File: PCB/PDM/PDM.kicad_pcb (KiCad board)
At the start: 2 copper layers, 42 parts, among them IC1 BTS70021EPPXUMA1, IC2 BTS70021EPPXUMA1, IC3 BTS500101TAEATMA1, IC4 TS5A21366DCUR, Q1 MMBT3904, U1 STM32F405RGTx, U2 MCP2561-E-SN, U3 MCP2561-E-SN

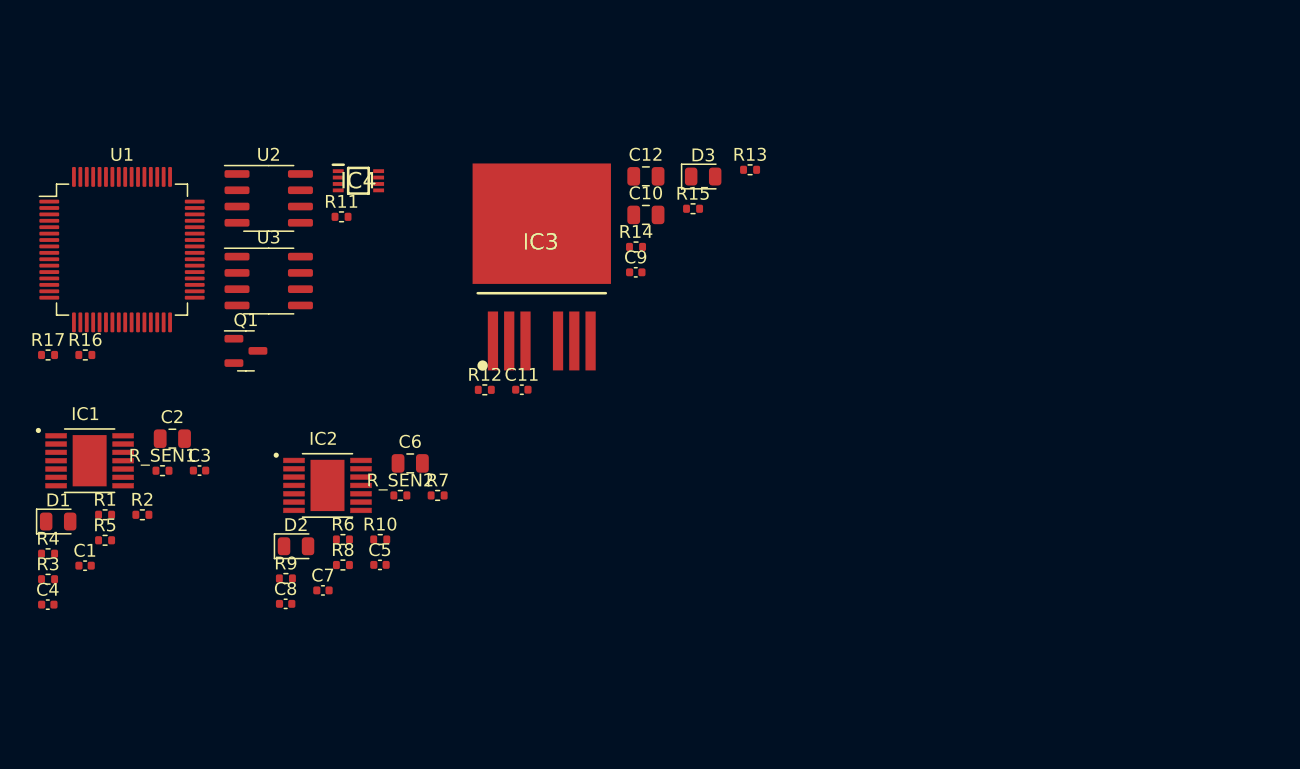
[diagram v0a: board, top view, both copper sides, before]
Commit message: Added another high-side switch 2x7A + 2x4A SPI
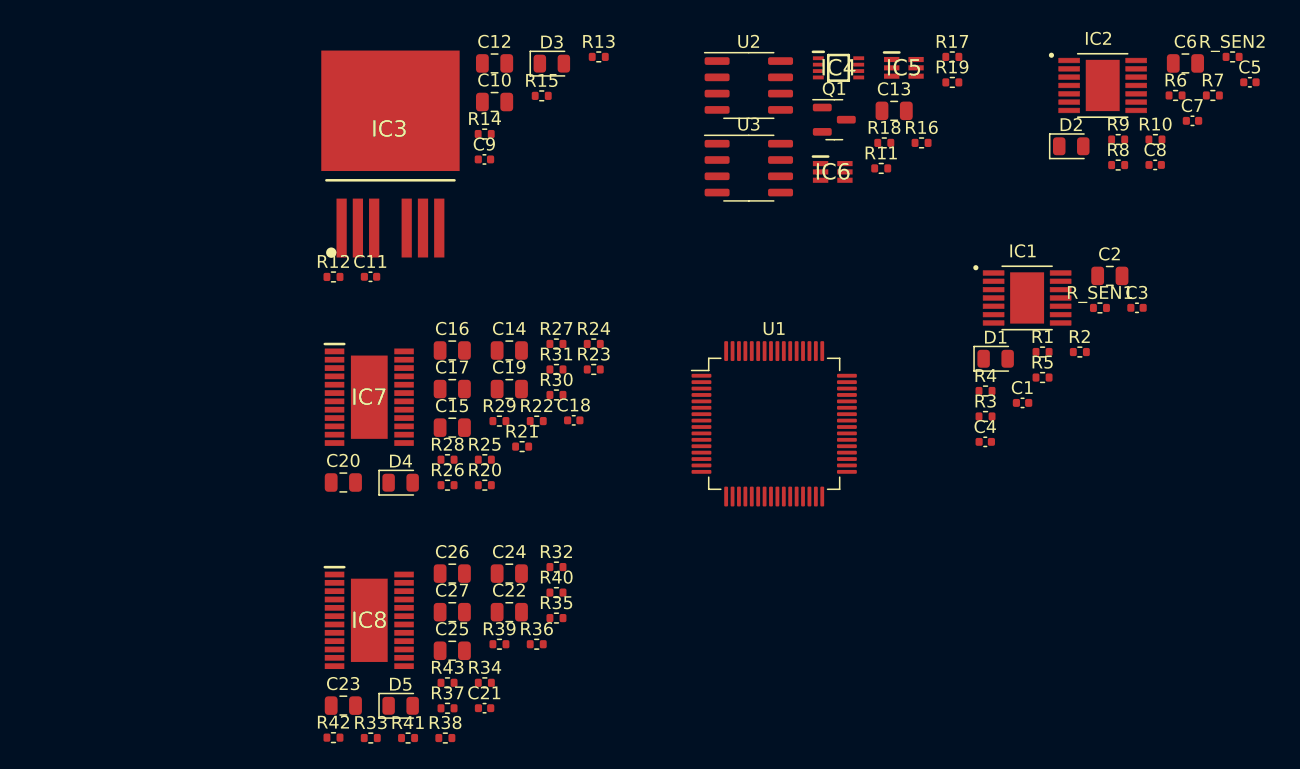
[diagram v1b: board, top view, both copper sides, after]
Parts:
- added C13: 0,1mF, Capacitor_SMD:C_0805_2012Metric, F.Cu at (245.5, 23.9)
- added C14: 10nf, Capacitor_SMD:C_0805_2012Metric, F.Cu at (215.5, 42.6)
- added C15: 10nf, Capacitor_SMD:C_0805_2012Metric, F.Cu at (211.0, 48.7)
- added C16: 10nf, Capacitor_SMD:C_0805_2012Metric, F.Cu at (211.0, 42.6)
- added C17: 10nf, Capacitor_SMD:C_0805_2012Metric, F.Cu at (211.0, 45.7)
- added C18: 220pF, Capacitor_SMD:C_0402_1005Metric, F.Cu at (220.5, 48.1)
- added C19: 470nF, Capacitor_SMD:C_0805_2012Metric, F.Cu at (215.5, 45.7)
- added C20: 100nF, Capacitor_SMD:C_0805_2012Metric, F.Cu at (202.5, 52.9)
- added C21: 220pF, Capacitor_SMD:C_0402_1005Metric, F.Cu at (213.5, 70.6)
- added C22: 470nF, Capacitor_SMD:C_0805_2012Metric, F.Cu at (215.5, 63.1)
- added C23: 100nF, Capacitor_SMD:C_0805_2012Metric, F.Cu at (202.5, 70.4)
- added C24: 10nf, Capacitor_SMD:C_0805_2012Metric, F.Cu at (215.5, 60.1)
- added C25: 10nf, Capacitor_SMD:C_0805_2012Metric, F.Cu at (211.0, 66.1)
- added C26: 10nf, Capacitor_SMD:C_0805_2012Metric, F.Cu at (211.0, 60.1)
- added C27: 10nf, Capacitor_SMD:C_0805_2012Metric, F.Cu at (211.0, 63.1)
- added D4: 7V, Diode_SMD:D_0805_2012Metric, F.Cu at (207.0, 53.0)
- added D5: 7V, Diode_SMD:D_0805_2012Metric, F.Cu at (207.0, 70.4)
- added IC5: TMP126NDCKR, PDM_Additional:SOT65P210X110-6N, F.Cu at (246.3, 20.6)
- added IC6: TMP126NDCKR, PDM_Additional:SOT65P210X110-6N, F.Cu at (240.7, 28.7)
- added IC7: BTS722204ESAXUMA1, PDM_Additional:SOP65P600X115-25N, F.Cu at (204.5, 46.3)
- added IC8: BTS722204ESAXUMA1, PDM_Additional:SOP65P600X115-25N, F.Cu at (204.5, 63.7)
- added R18: 10k, Resistor_SMD:R_0402_1005Metric, F.Cu at (244.7, 26.4)
- added R19: 10k, Resistor_SMD:R_0402_1005Metric, F.Cu at (250.0, 21.7)
- added R20: 1.2k, Resistor_SMD:R_0402_1005Metric, F.Cu at (213.6, 53.2)
- added R21: 1.2k, Resistor_SMD:R_0402_1005Metric, F.Cu at (216.5, 50.1)
- added R22: 1.2k, Resistor_SMD:R_0402_1005Metric, F.Cu at (217.6, 48.2)
- added R23: 1.2k, Resistor_SMD:R_0402_1005Metric, F.Cu at (222.1, 44.1)
- added R24: 4.7k, Resistor_SMD:R_0402_1005Metric, F.Cu at (222.1, 42.1)
- added R25: 4.7k, Resistor_SMD:R_0402_1005Metric, F.Cu at (213.6, 51.2)
- added R26: 4.7k, Resistor_SMD:R_0402_1005Metric, F.Cu at (210.7, 53.2)
- added R27: 4.7k, Resistor_SMD:R_0402_1005Metric, F.Cu at (219.2, 42.1)
- added R28: 47, Resistor_SMD:R_0402_1005Metric, F.Cu at (210.7, 51.2)
- added R29: 470, Resistor_SMD:R_0402_1005Metric, F.Cu at (214.7, 48.2)
- added R30: 4.7k, Resistor_SMD:R_0402_1005Metric, F.Cu at (219.2, 46.1)
- added R31: 1.2k, Resistor_SMD:R_0402_1005Metric, F.Cu at (219.2, 44.1)
- added R32: 47, Resistor_SMD:R_0402_1005Metric, F.Cu at (219.2, 59.5)
- added R33: 470, Resistor_SMD:R_0402_1005Metric, F.Cu at (204.7, 72.9)
- added R34: 4.7k, Resistor_SMD:R_0402_1005Metric, F.Cu at (213.6, 68.6)
- added R35: 1.2k, Resistor_SMD:R_0402_1005Metric, F.Cu at (219.2, 63.5)
- added R36: 1.2k, Resistor_SMD:R_0402_1005Metric, F.Cu at (217.6, 65.6)
- added R37: 1.2k, Resistor_SMD:R_0402_1005Metric, F.Cu at (210.7, 70.6)
- added R38: 1.2k, Resistor_SMD:R_0402_1005Metric, F.Cu at (210.5, 72.9)
- added R39: 4.7k, Resistor_SMD:R_0402_1005Metric, F.Cu at (214.7, 65.6)
- added R40: 4.7k, Resistor_SMD:R_0402_1005Metric, F.Cu at (219.2, 61.5)
- added R41: 4.7k, Resistor_SMD:R_0402_1005Metric, F.Cu at (207.6, 72.9)
- added R42: 4.7k, Resistor_SMD:R_0402_1005Metric, F.Cu at (201.8, 72.9)
- added R43: 1.2k, Resistor_SMD:R_0402_1005Metric, F.Cu at (210.7, 68.6)
- moved C5 77.6 mm to (273.3, 21.7)
- moved C7 77.1 mm to (268.8, 24.7)
- moved C8 76.0 mm to (265.9, 28.2)
- moved R17 74.3 mm to (250.0, 19.7)
- moved C2 74.2 mm to (262.3, 36.8)
- moved C3 74.2 mm to (264.5, 39.3)
- moved C4 74.2 mm to (252.6, 49.8)
- moved D1 74.2 mm to (253.4, 43.3)
- moved R1 74.2 mm to (257.1, 42.8)
- moved R2 74.2 mm to (260.0, 42.8)
- moved R5 74.2 mm to (257.1, 44.8)
- moved R_SEN1 74.2 mm to (261.6, 39.3)
- moved C1 74.2 mm to (255.5, 46.7)
- moved IC1 74.2 mm to (255.9, 38.5)
- moved R3 74.2 mm to (252.6, 47.8)
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
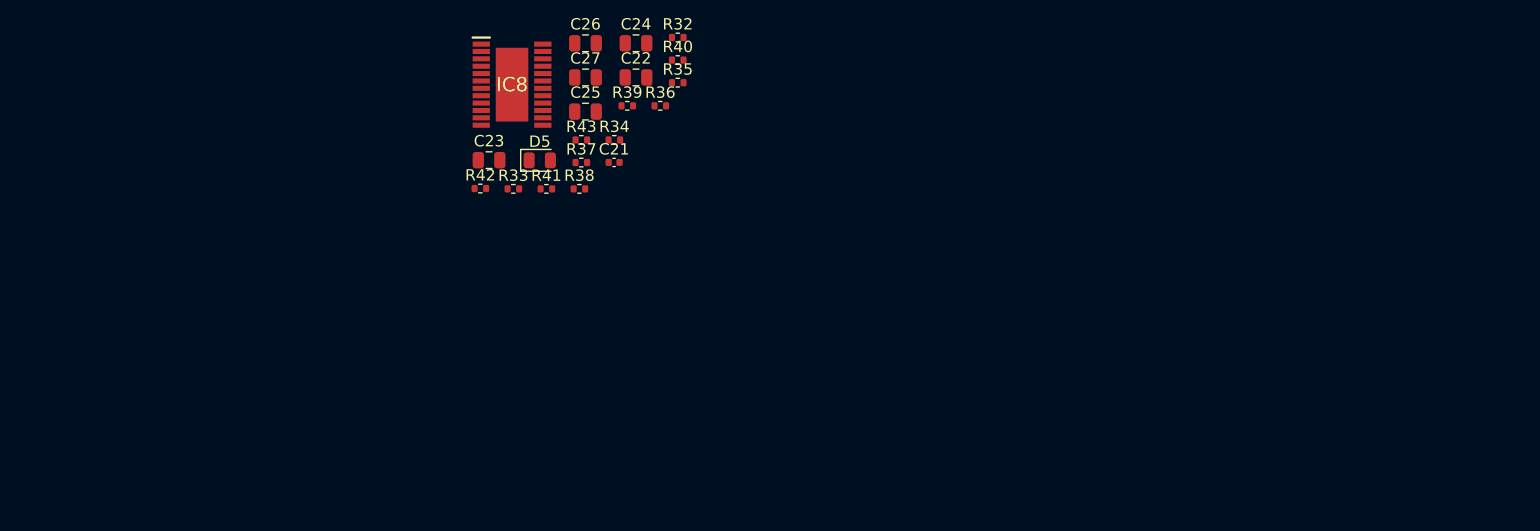
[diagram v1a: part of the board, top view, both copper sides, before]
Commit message: Added Reverse polarity protection
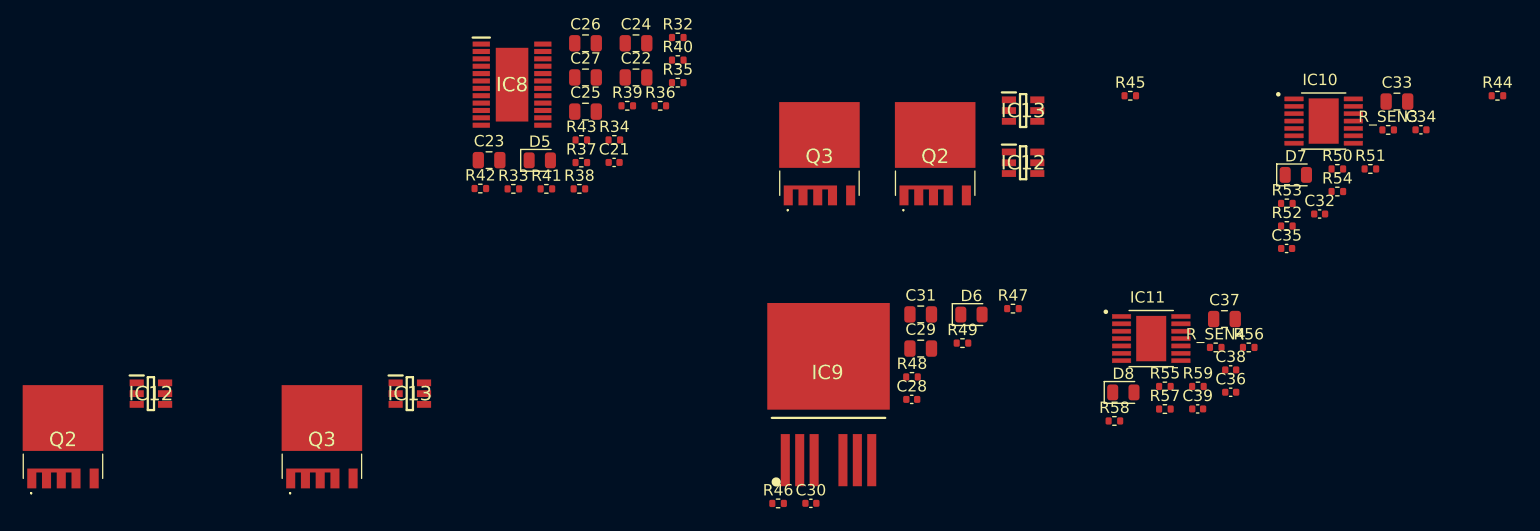
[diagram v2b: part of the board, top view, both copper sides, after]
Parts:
- added C28: 10nF, Capacitor_SMD:C_0402_1005Metric, F.Cu at (239.8, 91.4)
- added C29: 150nF, Capacitor_SMD:C_0805_2012Metric, F.Cu at (240.6, 87.0)
- added C30: 10nF, Capacitor_SMD:C_0402_1005Metric, F.Cu at (230.9, 100.6)
- added C31: 100nF, Capacitor_SMD:C_0805_2012Metric, F.Cu at (240.6, 84.0)
- added C32: 220pF, Capacitor_SMD:C_0402_1005Metric, F.Cu at (275.7, 75.1)
- added C33: 100nF, Capacitor_SMD:C_0805_2012Metric, F.Cu at (282.5, 65.2)
- added C34: 47nF, Capacitor_SMD:C_0402_1005Metric, F.Cu at (284.7, 67.7)
- added C35: 10nF, Capacitor_SMD:C_0402_1005Metric, F.Cu at (272.8, 78.1)
- added C36: 220pF, Capacitor_SMD:C_0402_1005Metric, F.Cu at (267.9, 90.8)
- added C37: 100nF, Capacitor_SMD:C_0805_2012Metric, F.Cu at (267.3, 84.4)
- added C38: 47nF, Capacitor_SMD:C_0402_1005Metric, F.Cu at (267.9, 88.8)
- added C39: 10nF, Capacitor_SMD:C_0402_1005Metric, F.Cu at (265.0, 92.3)
- added D6: 40V, Diode_SMD:D_0805_2012Metric, F.Cu at (245.0, 84.0)
- added D7: 7V, Diode_SMD:D_0805_2012Metric, F.Cu at (273.6, 71.7)
- added D8: 7V, Diode_SMD:D_0805_2012Metric, F.Cu at (258.4, 90.8)
- added IC10: BTS70021EPPXUMA1, PDM_Additional:SOP65P600X115-15N, F.Cu at (276.1, 66.9)
- added IC11: BTS70021EPPXUMA1, PDM_Additional:SOP65P600X115-15N, F.Cu at (260.9, 86.1)
- added IC12: LM5050MK-1_NOPB, PDM_Additional:SOT95P280X110-6N, F.Cu at (172.7, 90.9)
- added IC12: LM5050MK-1_NOPB, PDM_Additional:SOT95P280X110-6N, F.Cu at (249.6, 70.6)
- added IC13: LM5050MK-1_NOPB, PDM_Additional:SOT95P280X110-6N, F.Cu at (249.6, 66.0)
- added IC13: LM5050MK-1_NOPB, PDM_Additional:SOT95P280X110-6N, F.Cu at (195.5, 90.9)
- added IC9: BTS500101TAEATMA1, PDM_Additional:PG-TO263-7-3_3, F.Cu at (232.4, 87.6)
- added Q2: IAUA250N04S6N007AUMA1, PDM_Additional:IAUA250N04S6N007AUMA1, F.Cu at (241.8, 71.0)
- added Q2: IAUA250N04S6N007AUMA1, PDM_Additional:IAUA250N04S6N007AUMA1, F.Cu at (165.0, 96.0)
- added Q3: IAUA250N04S6N007AUMA1, PDM_Additional:IAUA250N04S6N007AUMA1, F.Cu at (231.6, 71.0)
- added Q3: IAUA250N04S6N007AUMA1, PDM_Additional:IAUA250N04S6N007AUMA1, F.Cu at (187.8, 96.0)
- added R44: 1.2k, Resistor_SMD:R_0402_1005Metric, F.Cu at (291.4, 64.7)
- added R45: 1.2k, Resistor_SMD:R_0402_1005Metric, F.Cu at (259.0, 64.7)
- added R46: 4.7k, Resistor_SMD:R_0402_1005Metric, F.Cu at (228.0, 100.6)
- added R47: 1k, Resistor_SMD:R_0402_1005Metric, F.Cu at (248.7, 83.4)
- added R48: 4.7k, Resistor_SMD:R_0402_1005Metric, F.Cu at (239.8, 89.5)
- added R49: 10, Resistor_SMD:R_0402_1005Metric, F.Cu at (244.2, 86.5)
- added R50: 4,7k, Resistor_SMD:R_0402_1005Metric, F.Cu at (277.3, 71.1)
- added R51: 4.7k, Resistor_SMD:R_0402_1005Metric, F.Cu at (280.2, 71.1)
- added R52: 4.7k, Resistor_SMD:R_0402_1005Metric, F.Cu at (272.8, 76.2)
- added R53: 4.7k, Resistor_SMD:R_0402_1005Metric, F.Cu at (272.8, 74.2)
- added R54: 47, Resistor_SMD:R_0402_1005Metric, F.Cu at (277.3, 73.1)
- added R55: 4,7k, Resistor_SMD:R_0402_1005Metric, F.Cu at (262.1, 90.3)
- added R56: 4.7k, Resistor_SMD:R_0402_1005Metric, F.Cu at (269.5, 86.9)
- added R57: 4.7k, Resistor_SMD:R_0402_1005Metric, F.Cu at (262.1, 92.3)
- added R58: 4.7k, Resistor_SMD:R_0402_1005Metric, F.Cu at (257.6, 93.3)
- added R59: 47, Resistor_SMD:R_0402_1005Metric, F.Cu at (265.0, 90.3)
- added R_SEN3: 1.2k, Resistor_SMD:R_0402_1005Metric, F.Cu at (281.8, 67.7)
- added R_SEN4: 1.2k, Resistor_SMD:R_0402_1005Metric, F.Cu at (266.6, 86.9)
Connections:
- IC7 pad 7: unconnected-(IC7-Pad7) -> Net-(IC7-Pad7)
- IC8 pad 7: unconnected-(IC8-Pad7) -> Net-(IC8-Pad7)

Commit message: Fuck christmas & low side section
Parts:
- removed the IC12 at (172.7, 90.9)
- removed the IC12 at (249.6, 70.6)
- removed the IC13 at (249.6, 66.0)
- removed the IC13 at (195.5, 90.9)
- removed the Q2 at (241.8, 71.0)
- removed the Q2 at (165.0, 96.0)
- removed the Q3 at (231.6, 71.0)
- removed the Q3 at (187.8, 96.0)
- added D10: WS2812B, LED_SMD:LED_WS2812B-2020_PLCC4_2.0x2.0mm, F.Cu at (179.9, 84.9)
- added D11: WS2812B, LED_SMD:LED_WS2812B-2020_PLCC4_2.0x2.0mm, F.Cu at (184.3, 81.9)
- added D9: WS2812B, LED_SMD:LED_WS2812B-2020_PLCC4_2.0x2.0mm, F.Cu at (185.2, 78.2)
- added IC12: LM5050MK-1_NOPB, PDM_Additional:SOT95P280X110-6N, F.Cu at (235.9, 68.2)
- added IC13: LM5050MK-1_NOPB, PDM_Additional:SOT95P280X110-6N, F.Cu at (257.5, 51.5)
- added IC14: TLE8104E, PDM_Additional:SOIC127P1030X255-21N, F.Cu at (200.3, 83.6)
- added Q2: IAUA250N04S6N007AUMA1, PDM_Additional:IAUA250N04S6N007AUMA1, F.Cu at (228.1, 73.3)
- added Q3: IAUA250N04S6N007AUMA1, PDM_Additional:IAUA250N04S6N007AUMA1, F.Cu at (249.8, 56.5)
- added R62: 1.2k, Resistor_SMD:R_0402_1005Metric, F.Cu at (208.2, 81.4)
- added R63: 4.7k, Resistor_SMD:R_0402_1005Metric, F.Cu at (211.1, 79.4)
- added R64: 4.7k, Resistor_SMD:R_0402_1005Metric, F.Cu at (208.2, 79.4)
- added R65: 4.7k, Resistor_SMD:R_0402_1005Metric, F.Cu at (211.1, 77.4)
- added R66: 4.7k, Resistor_SMD:R_0402_1005Metric, F.Cu at (208.2, 85.3)
- added R67: 1.2k, Resistor_SMD:R_0402_1005Metric, F.Cu at (208.2, 77.4)
- added R68: 1.2k, Resistor_SMD:R_0402_1005Metric, F.Cu at (211.1, 81.4)
- added R69: 1.2k, Resistor_SMD:R_0402_1005Metric, F.Cu at (208.2, 83.3)
- U1: value STM32F405RGTx -> STM32L496VGTx; footprint Package_QFP:LQFP-64_10x10mm_P0.5mm -> Package_QFP:LQFP-100_14x14mm_P0.5mm
- moved R17 102.7 mm to (174.4, 89.2)
- moved R19 96.9 mm to (179.0, 87.6)
- moved Q1 87.2 mm to (175.4, 82.3)
- moved IC5 87.2 mm to (180.8, 78.2)
- moved C13 87.2 mm to (180.0, 81.6)
- moved IC6 87.2 mm to (175.3, 86.4)
- moved U3 87.2 mm to (168.7, 86.1)
- moved IC4 87.2 mm to (175.7, 78.2)
- moved U2 87.2 mm to (168.7, 79.6)
- moved R44 86.9 mm to (204.5, 64.0)
- moved R11 83.0 mm to (183.4, 84.6)
- moved R16 79.2 mm to (188.7, 79.4)
- moved R18 75.7 mm to (188.7, 77.4)
- moved C28 68.3 mm to (177.7, 63.0)
- moved R46 68.3 mm to (165.9, 72.1)
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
